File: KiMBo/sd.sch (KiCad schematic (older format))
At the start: 9 parts

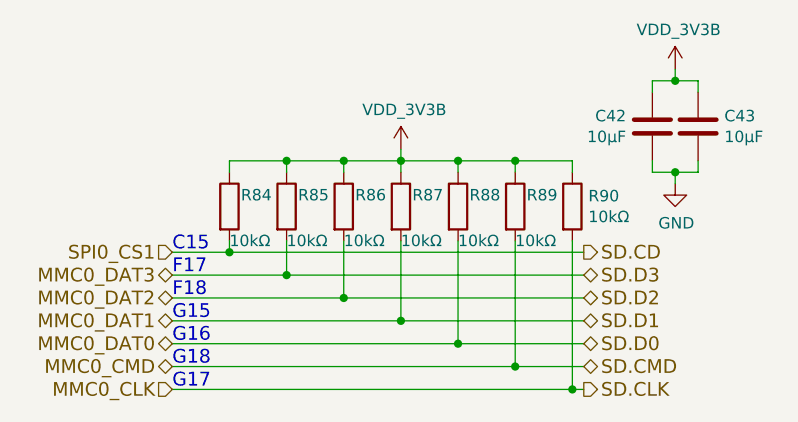
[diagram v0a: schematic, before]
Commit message: Leave SPI0 free for a display, reassign pins so SPI1 is available
Fix some typos/errors
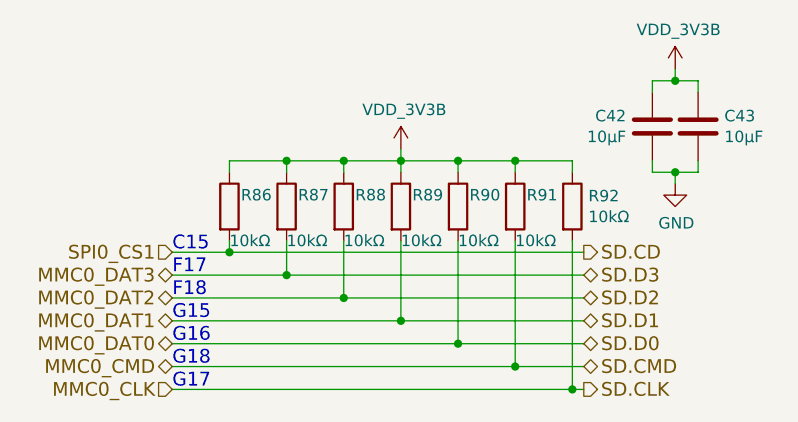
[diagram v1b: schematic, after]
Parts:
- renumbered R84 to R86, R85 to R87, R86 to R88, R87 to R89, R88 to R90, R89 to R91, R90 to R92
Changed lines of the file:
@@
 Connection ~ 7000 2950
 $Comp
-L GND #PWR0146
+L GND #PWR0145
 U 1 1 589C8FE8
 P 7000 3000
-F 0 "#PWR0146" H 7000 2750 50  0001 C CNN
+F 0 "#PWR0145" H 7000 2750 50  0001 C CNN
 F 1 "GND" H 7005 2827 50  0000 C CNN
 F 2 "" H 7000 3000 50  0000 C CNN
@@
 	4800 3900 6600 3900
 $Comp
-L R R85
+L R R87
 U 1 1 58F3951D
 P 5300 3100
-F 0 "R85" H 5350 3150 50  0000 L CNN
+F 0 "R87" H 5350 3150 50  0000 L CNN
 F 1 "10kΩ" H 5300 2950 50  0000 L CNN
 F 2 "Resistors_SMD:R_0402" V 5230 3100 50  0001 C CNN
@@
 $EndComp
 $Comp
-L R R86
+L R R88
 U 1 1 58F3959D
 P 5550 3100
-F 0 "R86" H 5600 3150 50  0000 L CNN
+F 0 "R88" H 5600 3150 50  0000 L CNN
 F 1 "10kΩ" H 5550 2950 50  0000 L CNN
 F 2 "Resistors_SMD:R_0402" V 5480 3100 50  0001 C CNN
@@
 $EndComp
 $Comp
-L R R87
+L R R89
 U 1 1 58F395D9
 P 5800 3100
-F 0 "R87" H 5850 3150 50  0000 L CNN
+F 0 "R89" H 5850 3150 50  0000 L CNN
 F 1 "10kΩ" H 5800 2950 50  0000 L CNN
 F 2 "Resistors_SMD:R_0402" V 5730 3100 50  0001 C CNN
@@
 $EndComp
 $Comp
-L R R88
+L R R90
 U 1 1 58F39A19
 P 6050 3100
-F 0 "R88" H 6100 3150 50  0000 L CNN
+F 0 "R90" H 6100 3150 50  0000 L CNN
 F 1 "10kΩ" H 6050 2950 50  0000 L CNN
 F 2 "Resistors_SMD:R_0402" V 5980 3100 50  0001 C CNN
@@
 $EndComp
 $Comp
-L R R89
+L R R91
 U 1 1 58F39B2F
 P 6300 3100
-F 0 "R89" H 6350 3150 50  0000 L CNN
+F 0 "R91" H 6350 3150 50  0000 L CNN
 F 1 "10kΩ" H 6300 2950 50  0000 L CNN
 F 2 "Resistors_SMD:R_0402" V 6230 3100 50  0001 C CNN
@@
 $EndComp
 $Comp
-L R R90
+L R R92
 U 1 1 58F39B72
 P 6550 3100
-F 0 "R90" H 6620 3146 50  0000 L CNN
+F 0 "R92" H 6620 3146 50  0000 L CNN
 F 1 "10kΩ" H 6620 3055 50  0000 L CNN
 F 2 "Resistors_SMD:R_0402" V 6480 3100 50  0001 C CNN
@@
 SPI0_CS1
 $Comp
-L R R84
+L R R86
 U 1 1 58F3C883
 P 5050 3100
-F 0 "R84" H 5100 3150 50  0000 L CNN
+F 0 "R86" H 5100 3150 50  0000 L CNN
 F 1 "10kΩ" H 5050 2950 50  0000 L CNN
 F 2 "Resistors_SMD:R_0402" V 4980 3100 50  0001 C CNN
@@
 G17
 $Comp
-L VDD_3V3B #PWR0147
+L VDD_3V3B #PWR0146
 U 1 1 5A066650
 P 5800 2850
-F 0 "#PWR0147" H 5800 2700 50  0001 C CNN
+F 0 "#PWR0146" H 5800 2700 50  0001 C CNN
 F 1 "VDD_3V3B" H 5815 3023 50  0000 C CNN
 F 2 "" H 5800 2850 50  0000 C CNN
@@
 $EndComp
 $Comp
-L VDD_3V3B #PWR0148
+L VDD_3V3B #PWR0147
 U 1 1 5A066680
 P 7000 2500
-F 0 "#PWR0148" H 7000 2350 50  0001 C CNN
+F 0 "#PWR0147" H 7000 2350 50  0001 C CNN
 F 1 "VDD_3V3B" H 7015 2673 50  0000 C CNN
 F 2 "" H 7000 2500 50  0000 C CNN

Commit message: Use fixed 5V LM2592HV Buck, include SPI0 header for LCD
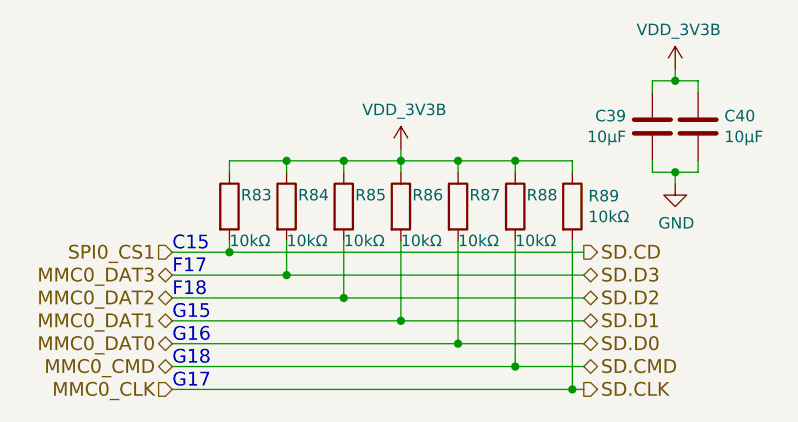
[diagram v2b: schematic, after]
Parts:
- renumbered C42 to C39, C43 to C40, R86 to R83, R87 to R84, R88 to R85, R89 to R86, R90 to R87, R91 to R88, R92 to R89
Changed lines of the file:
@@
 $EndDescr
 $Comp
-L C C42
+L C C39
 U 1 1 589C8DA1
 P 6900 2750
-F 0 "C42" H 7015 2796 50  0000 L CNN
+F 0 "C39" H 7015 2796 50  0000 L CNN
 F 1 "10μF" H 7015 2705 50  0000 L CNN
 F 2 "Capacitors_SMD:C_0603" H 6900 2750 50  0001 C CNN
@@
 $EndComp
 $Comp
-L C C43
+L C C40
 U 1 1 589C8DE9
 P 7100 2750
-F 0 "C43" H 7215 2796 50  0000 L CNN
+F 0 "C40" H 7215 2796 50  0000 L CNN
 F 1 "10μF" H 7215 2705 50  0000 L CNN
 F 2 "Capacitors_SMD:C_0603" H 7100 2750 50  0001 C CNN
@@
 Connection ~ 7000 2950
 $Comp
-L GND #PWR0145
+L GND #PWR0140
 U 1 1 589C8FE8
 P 7000 3000
-F 0 "#PWR0145" H 7000 2750 50  0001 C CNN
+F 0 "#PWR0140" H 7000 2750 50  0001 C CNN
 F 1 "GND" H 7005 2827 50  0000 C CNN
 F 2 "" H 7000 3000 50  0000 C CNN
@@
 	4800 3900 6600 3900
 $Comp
-L R R87
+L R R84
 U 1 1 58F3951D
 P 5300 3100
-F 0 "R87" H 5350 3150 50  0000 L CNN
+F 0 "R84" H 5350 3150 50  0000 L CNN
 F 1 "10kΩ" H 5300 2950 50  0000 L CNN
 F 2 "Resistors_SMD:R_0402" V 5230 3100 50  0001 C CNN
@@
 $EndComp
 $Comp
-L R R88
+L R R85
 U 1 1 58F3959D
 P 5550 3100
-F 0 "R88" H 5600 3150 50  0000 L CNN
+F 0 "R85" H 5600 3150 50  0000 L CNN
 F 1 "10kΩ" H 5550 2950 50  0000 L CNN
 F 2 "Resistors_SMD:R_0402" V 5480 3100 50  0001 C CNN
@@
 $EndComp
 $Comp
-L R R89
+L R R86
 U 1 1 58F395D9
 P 5800 3100
-F 0 "R89" H 5850 3150 50  0000 L CNN
+F 0 "R86" H 5850 3150 50  0000 L CNN
 F 1 "10kΩ" H 5800 2950 50  0000 L CNN
 F 2 "Resistors_SMD:R_0402" V 5730 3100 50  0001 C CNN
@@
 $EndComp
 $Comp
-L R R90
+L R R87
 U 1 1 58F39A19
 P 6050 3100
-F 0 "R90" H 6100 3150 50  0000 L CNN
+F 0 "R87" H 6100 3150 50  0000 L CNN
 F 1 "10kΩ" H 6050 2950 50  0000 L CNN
 F 2 "Resistors_SMD:R_0402" V 5980 3100 50  0001 C CNN
@@
 $EndComp
 $Comp
-L R R91
+L R R88
 U 1 1 58F39B2F
 P 6300 3100
-F 0 "R91" H 6350 3150 50  0000 L CNN
+F 0 "R88" H 6350 3150 50  0000 L CNN
 F 1 "10kΩ" H 6300 2950 50  0000 L CNN
 F 2 "Resistors_SMD:R_0402" V 6230 3100 50  0001 C CNN
@@
 $EndComp
 $Comp
-L R R92
+L R R89
 U 1 1 58F39B72
 P 6550 3100
-F 0 "R92" H 6620 3146 50  0000 L CNN
+F 0 "R89" H 6620 3146 50  0000 L CNN
 F 1 "10kΩ" H 6620 3055 50  0000 L CNN
 F 2 "Resistors_SMD:R_0402" V 6480 3100 50  0001 C CNN
@@
 SPI0_CS1
 $Comp
-L R R86
+L R R83
 U 1 1 58F3C883
 P 5050 3100
-F 0 "R86" H 5100 3150 50  0000 L CNN
+F 0 "R83" H 5100 3150 50  0000 L CNN
 F 1 "10kΩ" H 5050 2950 50  0000 L CNN
 F 2 "Resistors_SMD:R_0402" V 4980 3100 50  0001 C CNN
@@
 G17
 $Comp
-L VDD_3V3B #PWR0146
+L VDD_3V3B #PWR0141
 U 1 1 5A066650
 P 5800 2850
-F 0 "#PWR0146" H 5800 2700 50  0001 C CNN
+F 0 "#PWR0141" H 5800 2700 50  0001 C CNN
 F 1 "VDD_3V3B" H 5815 3023 50  0000 C CNN
 F 2 "" H 5800 2850 50  0000 C CNN
@@
 $EndComp
 $Comp
-L VDD_3V3B #PWR0147
+L VDD_3V3B #PWR0142
 U 1 1 5A066680
 P 7000 2500
-F 0 "#PWR0147" H 7000 2350 50  0001 C CNN
+F 0 "#PWR0142" H 7000 2350 50  0001 C CNN
 F 1 "VDD_3V3B" H 7015 2673 50  0000 C CNN
 F 2 "" H 7000 2500 50  0000 C CNN

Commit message: Assocate more footprints
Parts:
- R83, R84, R85, R86, R87, R88, R89: footprint Resistors_SMD:R_0402 -> Resistors_SMD:R_0603
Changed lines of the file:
@@
 F 0 "R84" H 5350 3150 50  0000 L CNN
 F 1 "10kΩ" H 5300 2950 50  0000 L CNN
-F 2 "Resistors_SMD:R_0402" V 5230 3100 50  0001 C CNN
+F 2 "Resistors_SMD:R_0603" V 5230 3100 50  0001 C CNN
 F 3 "" H 5300 3100 50  0000 C CNN
 	1    5300 3100
@@
 F 0 "R85" H 5600 3150 50  0000 L CNN
 F 1 "10kΩ" H 5550 2950 50  0000 L CNN
-F 2 "Resistors_SMD:R_0402" V 5480 3100 50  0001 C CNN
+F 2 "Resistors_SMD:R_0603" V 5480 3100 50  0001 C CNN
 F 3 "" H 5550 3100 50  0000 C CNN
 	1    5550 3100
@@
 F 0 "R86" H 5850 3150 50  0000 L CNN
 F 1 "10kΩ" H 5800 2950 50  0000 L CNN
-F 2 "Resistors_SMD:R_0402" V 5730 3100 50  0001 C CNN
+F 2 "Resistors_SMD:R_0603" V 5730 3100 50  0001 C CNN
 F 3 "" H 5800 3100 50  0000 C CNN
 	1    5800 3100
@@
 F 0 "R87" H 6100 3150 50  0000 L CNN
 F 1 "10kΩ" H 6050 2950 50  0000 L CNN
-F 2 "Resistors_SMD:R_0402" V 5980 3100 50  0001 C CNN
+F 2 "Resistors_SMD:R_0603" V 5980 3100 50  0001 C CNN
 F 3 "" H 6050 3100 50  0000 C CNN
 	1    6050 3100
@@
 F 0 "R88" H 6350 3150 50  0000 L CNN
 F 1 "10kΩ" H 6300 2950 50  0000 L CNN
-F 2 "Resistors_SMD:R_0402" V 6230 3100 50  0001 C CNN
+F 2 "Resistors_SMD:R_0603" V 6230 3100 50  0001 C CNN
 F 3 "" H 6300 3100 50  0000 C CNN
 	1    6300 3100
@@
 F 0 "R89" H 6620 3146 50  0000 L CNN
 F 1 "10kΩ" H 6620 3055 50  0000 L CNN
-F 2 "Resistors_SMD:R_0402" V 6480 3100 50  0001 C CNN
+F 2 "Resistors_SMD:R_0603" V 6480 3100 50  0001 C CNN
 F 3 "" H 6550 3100 50  0000 C CNN
 	1    6550 3100
@@
 F 0 "R83" H 5100 3150 50  0000 L CNN
 F 1 "10kΩ" H 5050 2950 50  0000 L CNN
-F 2 "Resistors_SMD:R_0402" V 4980 3100 50  0001 C CNN
+F 2 "Resistors_SMD:R_0603" V 4980 3100 50  0001 C CNN
 F 3 "" H 5050 3100 50  0000 C CNN
 	1    5050 3100

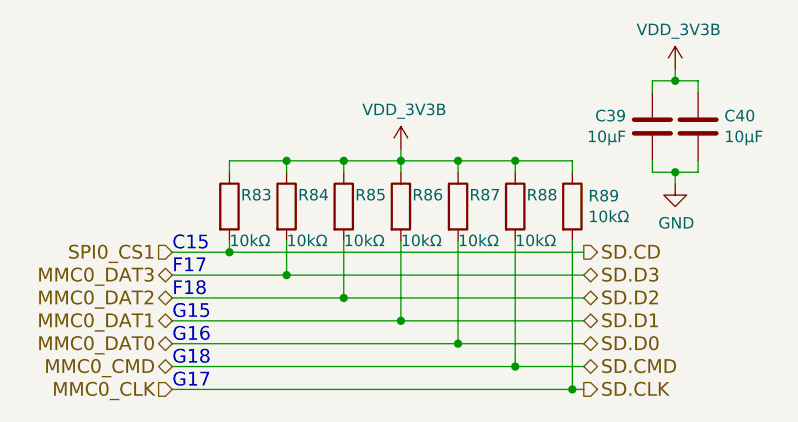
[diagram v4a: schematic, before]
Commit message: Begin layout
Arrange all connectors to get a feel for the area.
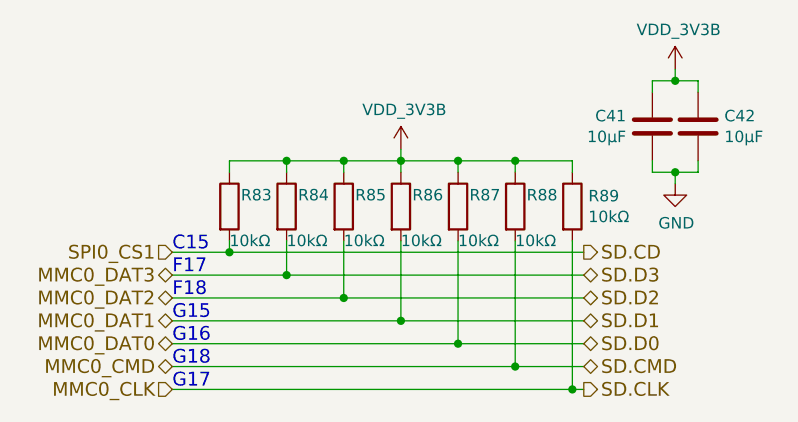
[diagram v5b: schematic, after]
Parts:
- renumbered C39 to C41, C40 to C42
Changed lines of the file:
@@
 $EndDescr
 $Comp
-L C C39
+L C C41
 U 1 1 589C8DA1
 P 6900 2750
-F 0 "C39" H 7015 2796 50  0000 L CNN
+F 0 "C41" H 7015 2796 50  0000 L CNN
 F 1 "10μF" H 7015 2705 50  0000 L CNN
 F 2 "Capacitors_SMD:C_0603" H 6900 2750 50  0001 C CNN
@@
 $EndComp
 $Comp
-L C C40
+L C C42
 U 1 1 589C8DE9
 P 7100 2750
-F 0 "C40" H 7215 2796 50  0000 L CNN
+F 0 "C42" H 7215 2796 50  0000 L CNN
 F 1 "10μF" H 7215 2705 50  0000 L CNN
 F 2 "Capacitors_SMD:C_0603" H 7100 2750 50  0001 C CNN
@@
 Connection ~ 7000 2950
 $Comp
-L GND #PWR0141
+L GND #PWR0144
 U 1 1 589C8FE8
 P 7000 3000
-F 0 "#PWR0141" H 7000 2750 50  0001 C CNN
+F 0 "#PWR0144" H 7000 2750 50  0001 C CNN
 F 1 "GND" H 7005 2827 50  0000 C CNN
 F 2 "" H 7000 3000 50  0000 C CNN
@@
 G17
 $Comp
-L VDD_3V3B #PWR0142
+L VDD_3V3B #PWR0145
 U 1 1 5A066650
 P 5800 2850
-F 0 "#PWR0142" H 5800 2700 50  0001 C CNN
+F 0 "#PWR0145" H 5800 2700 50  0001 C CNN
 F 1 "VDD_3V3B" H 5815 3023 50  0000 C CNN
 F 2 "" H 5800 2850 50  0000 C CNN
@@
 $EndComp
 $Comp
-L VDD_3V3B #PWR0143
+L VDD_3V3B #PWR0146
 U 1 1 5A066680
 P 7000 2500
-F 0 "#PWR0143" H 7000 2350 50  0001 C CNN
+F 0 "#PWR0146" H 7000 2350 50  0001 C CNN
 F 1 "VDD_3V3B" H 7015 2673 50  0000 C CNN
 F 2 "" H 7000 2500 50  0000 C CNN

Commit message: Remove HDMI from the schematic
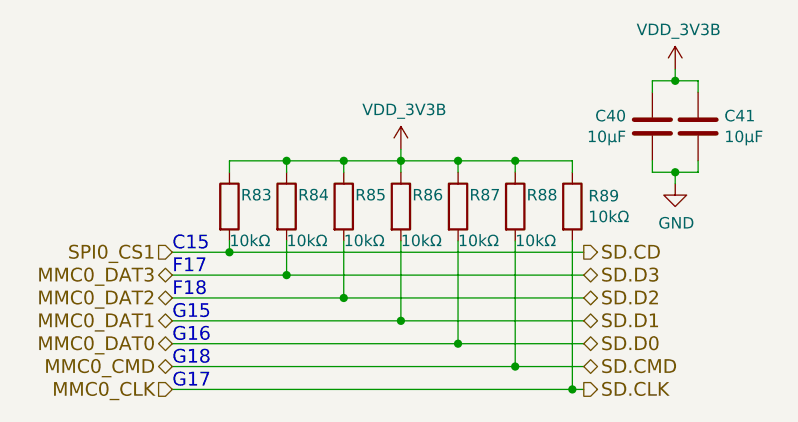
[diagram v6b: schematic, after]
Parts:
- renumbered C41 to C40, C42 to C41
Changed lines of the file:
@@
 $Descr A4 11693 8268
 encoding utf-8
-Sheet 9 26
+Sheet 9 25
 Title ""
 Date ""
@@
 $EndDescr
 $Comp
-L C C41
+L C C40
 U 1 1 589C8DA1
 P 6900 2750
-F 0 "C41" H 7015 2796 50  0000 L CNN
+F 0 "C40" H 7015 2796 50  0000 L CNN
 F 1 "10μF" H 7015 2705 50  0000 L CNN
 F 2 "Capacitors_SMD:C_0603" H 6900 2750 50  0001 C CNN
@@
 $EndComp
 $Comp
-L C C42
+L C C41
 U 1 1 589C8DE9
 P 7100 2750
-F 0 "C42" H 7215 2796 50  0000 L CNN
+F 0 "C41" H 7215 2796 50  0000 L CNN
 F 1 "10μF" H 7215 2705 50  0000 L CNN
 F 2 "Capacitors_SMD:C_0603" H 7100 2750 50  0001 C CNN
@@
 Connection ~ 7000 2950
 $Comp
-L GND #PWR0144
+L GND #PWR0139
 U 1 1 589C8FE8
 P 7000 3000
-F 0 "#PWR0144" H 7000 2750 50  0001 C CNN
+F 0 "#PWR0139" H 7000 2750 50  0001 C CNN
 F 1 "GND" H 7005 2827 50  0000 C CNN
 F 2 "" H 7000 3000 50  0000 C CNN
@@
 G17
 $Comp
-L VDD_3V3B #PWR0145
+L VDD_3V3B #PWR0140
 U 1 1 5A066650
 P 5800 2850
-F 0 "#PWR0145" H 5800 2700 50  0001 C CNN
+F 0 "#PWR0140" H 5800 2700 50  0001 C CNN
 F 1 "VDD_3V3B" H 5815 3023 50  0000 C CNN
 F 2 "" H 5800 2850 50  0000 C CNN
@@
 $EndComp
 $Comp
-L VDD_3V3B #PWR0146
+L VDD_3V3B #PWR0141
 U 1 1 5A066680
 P 7000 2500
-F 0 "#PWR0146" H 7000 2350 50  0001 C CNN
+F 0 "#PWR0141" H 7000 2350 50  0001 C CNN
 F 1 "VDD_3V3B" H 7015 2673 50  0000 C CNN
 F 2 "" H 7000 2500 50  0000 C CNN
